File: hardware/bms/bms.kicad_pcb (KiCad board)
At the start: 4 copper layers, 120 x 45 mm, 269 parts, among them J1 Screw_Terminal_01x01, J10 Conn_01x10, J11 USB_C_Receptacle_USB2.0, J12 Conn_01x03, J13 Conn_01x07, J2 Screw_Terminal_01x01, J3 Screw_Terminal_01x01, J4 Screw_Terminal_01x01, J5 Screw_Terminal_01x01, J6 Conn_01x02, J7 Conn_01x10, J8 Conn_01x02, Q1 MMBT3904, Q2 Q_PMOS_GDS, Q3 Q_PMOS_GDS, Q4 BSZ018N04LS6ATMA1, Q5 IAUC120N04S6N006ATMA1, Q6 IAUC120N04S6N006ATMA1, Q7 BSZ018N04LS6ATMA1, Q8 BSZ018N04LS6ATMA1, Q9 BSZ018N04LS6ATMA1, SW1 SW_SPST, SW2 SW_Push, SW3 SW_Push, U1 BQ76952, U2 LM74700, U3 BQ24610, U4 LM5166X, U5 TPS62172DSG, U6 ESP32-C3-MINI-1-N4, U7 SN74LXC1T14DCKR, U8 USBLC6-2SC6

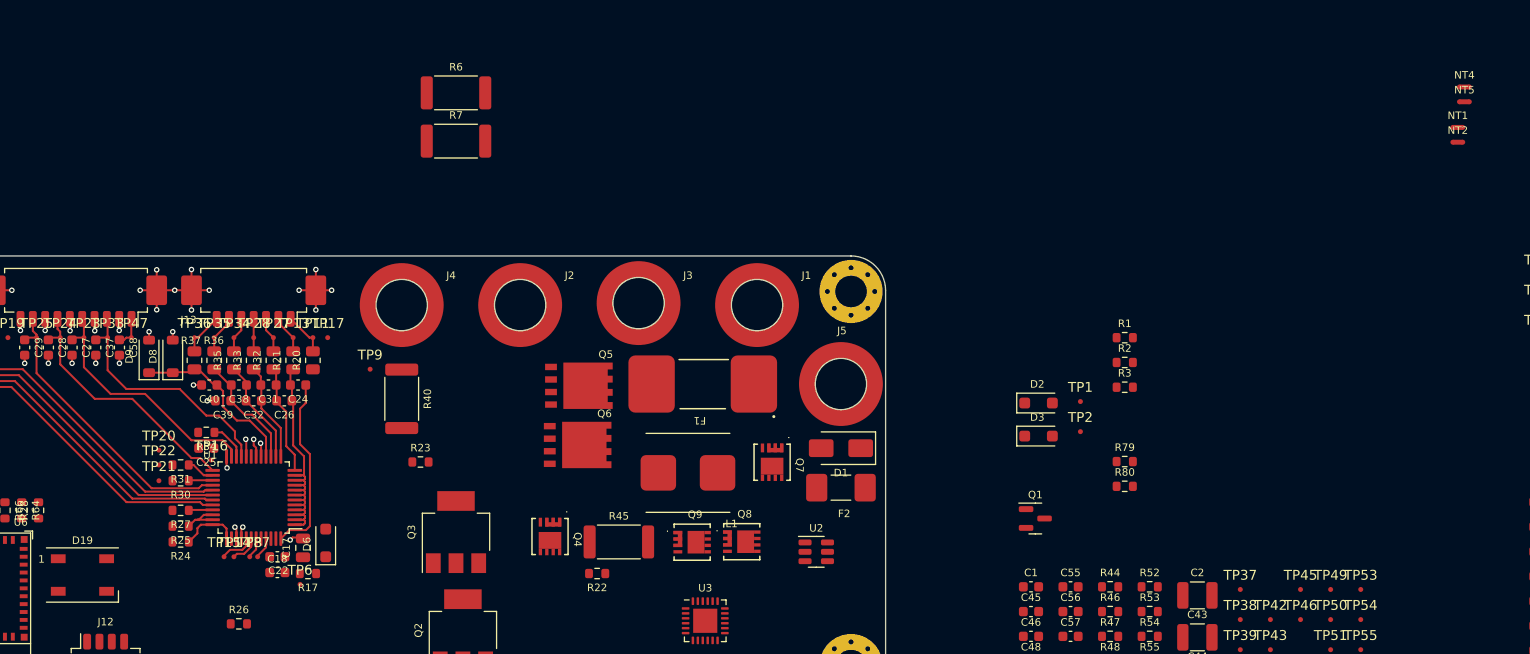
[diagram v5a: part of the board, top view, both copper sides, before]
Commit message: refined routing near cell taps
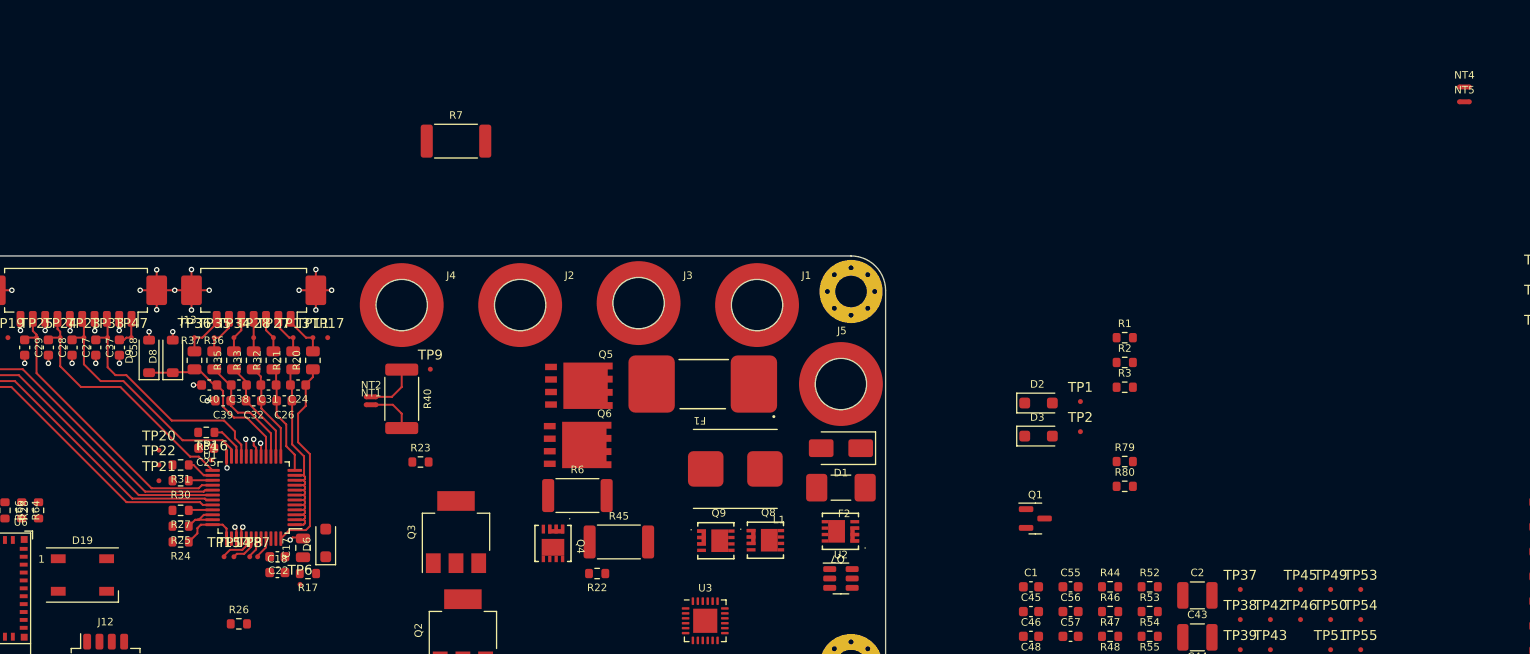
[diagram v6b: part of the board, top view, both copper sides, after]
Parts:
- moved NT1 113.6 mm to (156.7, 90.1)
- moved NT2 113.1 mm to (156.7, 89.3)
- moved R6 42.6 mm to (177.6, 99.3)
- moved Q7 9.85 mm to (204.2, 102.9), turned to 180 degrees
- moved TP9 6.10 mm to (162.7, 86.5)
- moved L1 4.82 mm to (193.6, 96.6)
- moved U2 3.68 mm to (204.2, 107.7)
- moved Q8 2.40 mm to (196.6, 103.8)
- moved Q9 2.40 mm to (191.6, 103.9)
- moved Q4 0.76 mm to (175.1, 104.2)
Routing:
- net /BATTERY BALANCE AND MONITOR/PACK-: track 0.00 -> 4.78 mm
- net GND: track 69.3 -> 73.8 mm
- net /BATTERY BALANCE AND MONITOR/VC16: track 18.4 -> 20.5 mm

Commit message: More layout, changed precharge / predischarged PMOS selection to SOT-23 size to save space. Charger layout will be difficult, may need to change charger input terminal location...
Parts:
- removed C15, C16: 0.1uF, Capacitor_SMD:C_0805_2012Metric
- D4, D5: footprint Diode_SMD:D_SOD-123 -> Diode_SMD:D_SOD-523
- NT1, NT2, NT4, NT5: footprint NetTie:NetTie-2_SMD_Pad0.5mm -> bms:NetTie-2_SMD_Pad_8mil
- Q2, Q3: value Q_PMOS_GDS -> Q_PMOS_GSD; footprint Package_TO_SOT_SMD:SOT-223-3_TabPin2 -> Package_TO_SOT_SMD:SOT-23
- moved D5 325.5 mm to (1.32, 0.72)
- moved R18 153.6 mm to (143.2, 107.6), turned to 90 degrees
- moved C33 144.2 mm to (139.9, 91.3), turned to 180 degrees
- moved R15 143.0 mm to (144.8, 107.6), turned to 90 degrees
- moved C19 142.4 mm to (165.8, 81.8), turned to -90 degrees
- moved R39 141.2 mm to (152.8, 91.8), turned to 90 degrees
- moved C21 140.9 mm to (165.8, 78.3), turned to -90 degrees
- moved R38 140.1 mm to (154.4, 91.8), turned to 90 degrees
- moved C42 136.9 mm to (153.7, 95.8)
- moved D4 133.6 mm to (181.4, 92.0), turned to 180 degrees
- moved C14 127.3 mm to (176.1, 84.5), turned to 180 degrees
- moved C41 127.2 mm to (153.7, 94.2)
- moved C13 124.4 mm to (179.6, 84.5), turned to 180 degrees
- moved C20 118.3 mm to (189.8, 81.8), turned to -90 degrees
- moved C23 116.7 mm to (189.8, 78.3), turned to -90 degrees
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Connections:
- Q2 pad 2: Net-(Q2-D) -> /BATTERY BALANCE AND MONITOR/VCHG+
- Q2 pad 3: /BATTERY BALANCE AND MONITOR/VCHG+ -> Net-(Q2-D)
- Q3 pad 2: Net-(Q3-D) -> /VBAT_IN_F
- Q3 pad 3: /VBAT_IN_F -> Net-(Q3-D)
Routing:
- net /BATTERY BALANCE AND MONITOR/SRP: track 1.84 -> 18.7 mm, vias 1 -> 2
- net /BATTERY BALANCE AND MONITOR/SRN: track 1.76 -> 18.4 mm, vias 1 -> 2
- net /BATTERY BALANCE AND MONITOR/DGATE: track 0.00 -> 16.4 mm, vias 0 -> 2
- net /BATTERY BALANCE AND MONITOR/PACK+: track 0.00 -> 10.5 mm, vias 0 -> 2
- net /BATTERY BALANCE AND MONITOR/PDGATE: track 0.00 -> 6.62 mm, vias 0 -> 2
- net Net-(NT2-Pad1): track 0.00 -> 3.95 mm
- net Net-(NT1-Pad1): track 0.00 -> 2.64 mm
- net Net-(Q6-G): track 0.00 -> 2.03 mm
- net Net-(Q5-G): track 0.00 -> 1.96 mm
- net /BATTERY BALANCE AND MONITOR/DSG: track 2.11 -> 4.01 mm
- net /BMS_WAKE: track 0.00 -> 1.62 mm
- net GND: track 73.8 -> 75.3 mm, vias 46 -> 47
- net /BATTERY BALANCE AND MONITOR/CHG: track 2.19 -> 3.59 mm
- net /BATTERY BALANCE AND MONITOR/PDSG: track 1.22 -> 1.80 mm, vias 1 -> 2

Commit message: Changed large input fuse, slightly smaller and cheaper, 60A rated. Layout more defined, charger layout much better now
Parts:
- removed R43, R46: 0R, Resistor_SMD:R_0603_1608Metric
- C47: footprint Capacitor_SMD:C_0805_2012Metric -> Capacitor_SMD:C_0603_1608Metric; moved to B.Cu
- C48, C53, C55, C56, C57, C58, D11, D4, D5, R10, R11, R12, R13, R14, R16, R22, R44, R47, R48, R51, R52, R8, R9: moved to B.Cu
- F1: value 80A -> 60A; footprint bms:FUSE_0ACH-9800-TE_BEL -> bms:SF-3812F6000T-2
- moved D5 209.6 mm to (187.8, 96.4)
- moved D7 117.7 mm to (177.8, 78.3), turned to -90 degrees
- moved R19 112.3 mm to (177.8, 81.5), turned to 90 degrees
- moved R8 110.0 mm to (184.7, 102.8), turned to -90 degrees
- moved R10 109.3 mm to (183.1, 102.8), turned to -90 degrees
- moved R13 102.6 mm to (185.1, 96.4)
- moved NT5 73.7 mm to (199.6, 88.3)
- moved NT4 70.7 mm to (203.6, 88.3), turned to 180 degrees
- moved C47 64.3 mm to (195.5, 100.9), turned to 180 degrees
- moved D11 63.3 mm to (196.4, 103.1), turned to -90 degrees
- moved C58 63.1 mm to (192.4, 99.3), turned to 180 degrees
- moved R51 49.8 mm to (192.4, 92.9)
- moved R52 44.5 mm to (192.4, 97.7)
- moved R47 43.5 mm to (192.4, 94.5), turned to 180 degrees
- moved R48 40.4 mm to (195.5, 97.7)
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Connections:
- Q8 pad 2: /BATTERY CHARGER/GH -> /BATTERY CHARGER/DRV_HI
- Q9 pad 2: /BATTERY CHARGER/GL -> /BATTERY CHARGER/DRV_LO
- TP40 pad 1: /BATTERY CHARGER/GH -> /BATTERY CHARGER/DRV_HI
- TP44 pad 1: /BATTERY CHARGER/GL -> /BATTERY CHARGER/DRV_LO
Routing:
- net /BATTERY CHARGER/SRN_CHG: track 0.00 -> 24.8 mm, vias 0 -> 2
- net /BATTERY CHARGER/SRP_CHG: track 0.00 -> 24.8 mm, vias 0 -> 2
- net /BATTERY BALANCE AND MONITOR/DGATE: track 16.4 -> 0.00 mm, vias 2 -> 0
- net /BATTERY CHARGER/DRV_LO: track 0.00 -> 12.9 mm, vias 0 -> 2
- net /BATTERY BALANCE AND MONITOR/PACK+: track 10.5 -> 0.00 mm, vias 2 -> 0
- net Net-(U2-EN): track 0.00 -> 7.28 mm
- net /BATTERY BALANCE AND MONITOR/PDGATE: track 6.62 -> 0.00 mm, vias 2 -> 0
- net /BATTERY CHARGER/SW_NODE: track 0.00 -> 5.42 mm, vias 0 -> 2
- net /BATTERY CHARGER/DRV_HI: track 0.00 -> 4.10 mm
- net /BATTERY CHARGER/C_VCC: track 0.00 -> 3.44 mm, vias 0 -> 1
- net /BATTERY BALANCE AND MONITOR/VCHG+: track 0.00 -> 3.23 mm
- net Net-(L1-Pad2): track 0.00 -> 3.03 mm
- net /BATTERY CHARGER/BTST: track 0.00 -> 2.68 mm, vias 0 -> 1
- net /BATTERY CHARGER/DG: track 0.00 -> 2.47 mm
- net /BATTERY CHARGER/REGEN: track 0.00 -> 2.20 mm, vias 0 -> 1
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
